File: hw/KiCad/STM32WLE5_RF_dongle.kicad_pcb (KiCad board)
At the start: 4 copper layers, 59 x 18 mm, 68 parts, among them J1 Conn_01x02_Pin, J2 cortex-M_debug_connector_10pin, J3 S0941-46R, J4 S0941-46R, J5 S0941-46R, J6 S0941-46R, J7 SMA_142-0701-801_EdgeMount, J8 USB_male_typeA_2.0, T1 DXW21HN5011BL, U1 STM32WLE5C8U6, U2 SKY13453-385LF, U3 USBLC6-2SC6, U4 FT230XS-R, U5 TLV75533PDBVR, Y1 ECS-TXO-25CSMV

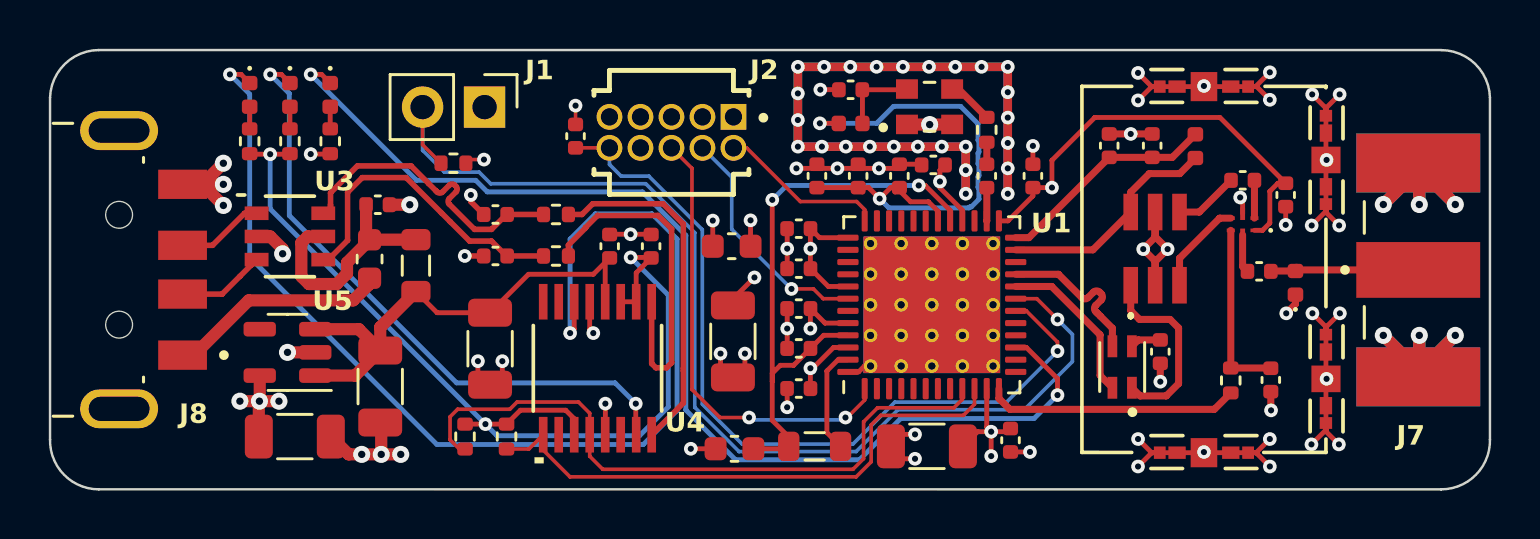
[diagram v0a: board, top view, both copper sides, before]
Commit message: Update PCB tracing according to PCBWay engineering team stackup definition and feedback
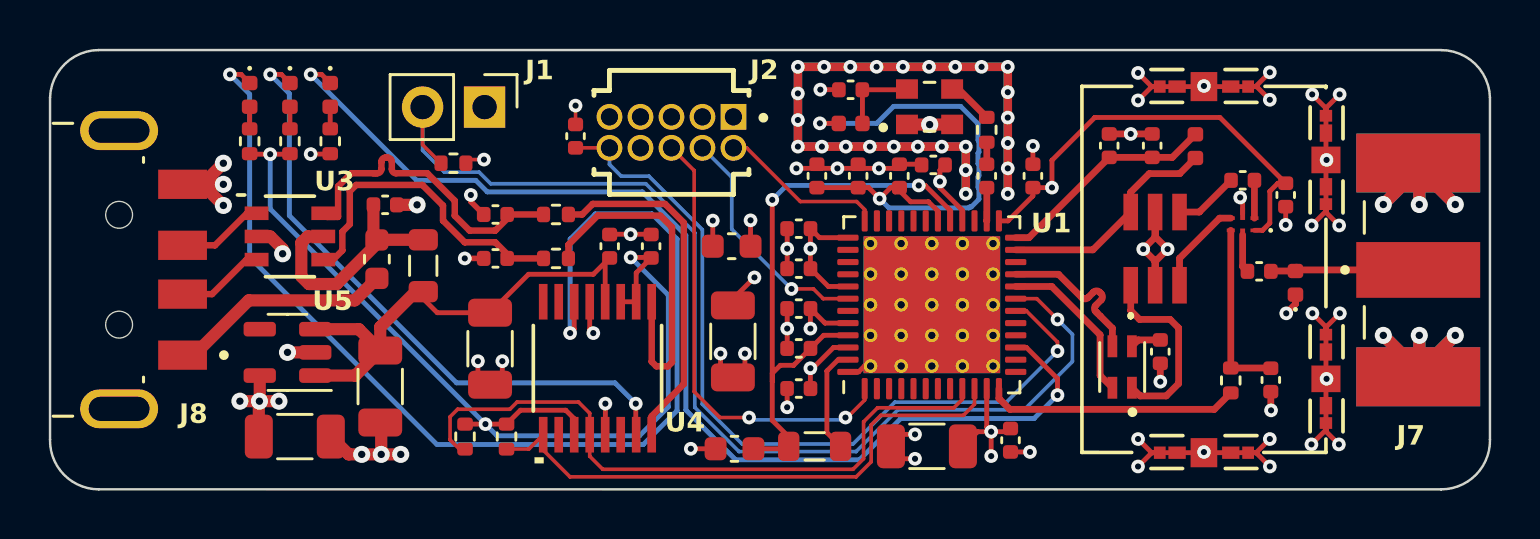
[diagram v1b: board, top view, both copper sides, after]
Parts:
- moved C31 0.30 mm to (108.0, 83.9)
- moved F1 0.30 mm to (107.7, 86.1)
- moved FB2 0.30 mm to (109.6, 86.3)
- moved C33 0.10 mm to (112.6, 86.0)
- moved R10 0.10 mm to (115.0, 86.0)
